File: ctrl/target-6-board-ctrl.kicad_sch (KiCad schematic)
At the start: 17 parts, among them J1 RJ25, Q1 2SC1815, Q2 2SC1815, Q3 2SC1815

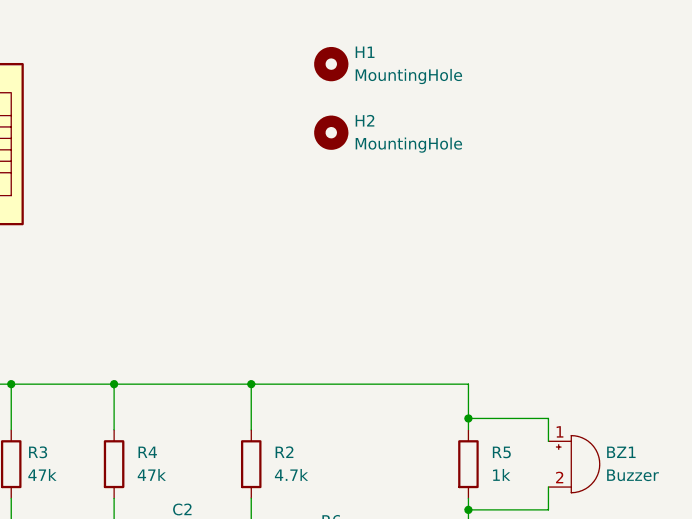
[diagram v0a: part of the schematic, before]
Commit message: ctrl: add mouting hole and board name and version
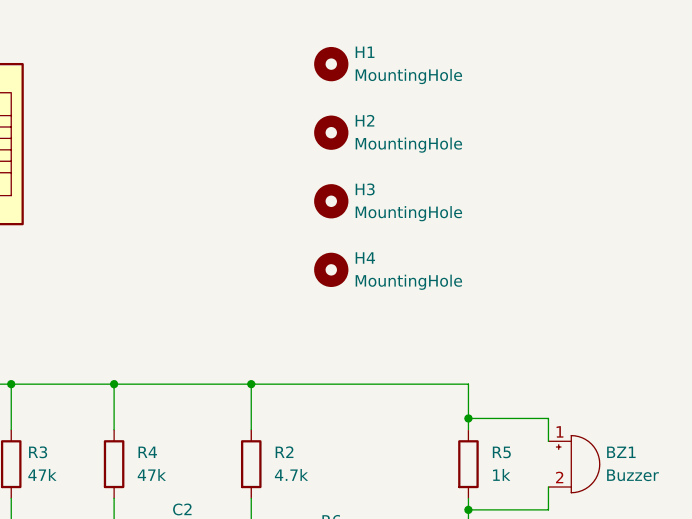
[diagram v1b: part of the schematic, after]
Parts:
- added H3, H4: MountingHole, MountingHole:MountingHole_3.2mm_M3, symbol Mechanical:MountingHole
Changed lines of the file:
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@@
+    )
+  )
+  (symbol (lib_id "Mechanical:MountingHole") (at 92.71 34.29 0) (unit 1)
+    (in_bom yes) (on_board yes) (dnp no) (fields_autoplaced)
+    (property "Reference" "H3" (at 95.25 33.02 0)
+      (effects (font (size 1.27 1.27)) (justify left))
+    )
+    (property "Value" "MountingHole" (at 95.25 35.56 0)
+      (effects (font (size 1.27 1.27)) (justify left))
+    )
+    (property "Footprint" "MountingHole:MountingHole_3.2mm_M3" (at 92.71 34.29 0)
+      (effects (font (size 1.27 1.27)) hide)
+    )
+    (property "Datasheet" "~" (at 92.71 34.29 0)
+      (effects (font (size 1.27 1.27)) hide)
+    )
+    (instances
+      (project "target-6-board-ctrl"
+        (path "/b19b5d92-02a7-4a53-88b8-2c17b82496f5"
+          (reference "H3") (unit 1)
+        )
+      )
     )
   )
@@
         )
       )
+    )
+  )
+  (symbol (lib_id "Mechanical:MountingHole") (at 92.71 41.91 0) (unit 1)
+    (in_bom yes) (on_board yes) (dnp no) (fields_autoplaced)
+    (property "Reference" "H4" (at 95.25 40.64 0)
+      (effects (font (size 1.27 1.27)) (justify left))
+    )
+    (property "Value" "MountingHole" (at 95.25 43.18 0)
+      (effects (font (size 1.27 1.27)) (justify left))
+    )
+    (property "Footprint" "MountingHole:MountingHole_3.2mm_M3" (at 92.71 41.91 0)
+      (effects (font (size 1.27 1.27)) hide)
+    )
+    (property "Datasheet" "~" (at 92.71 41.91 0)
+      (effects (font (size 1.27 1.27)) hide)
+    )
+    (instances
+      (project "target-6-board-ctrl"
+        (path "/b19b5d92-02a7-4a53-88b8-2c17b82496f5"
+          (reference "H4") (unit 1)
+        )
+      )
